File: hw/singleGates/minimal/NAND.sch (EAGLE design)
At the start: 5 parts, among them Q1 BC817, Q2 BC817

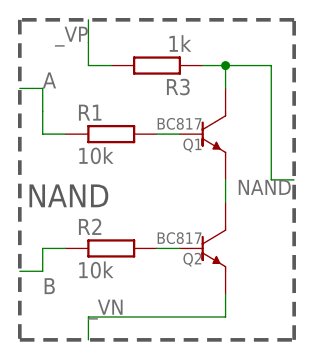
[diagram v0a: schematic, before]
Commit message: Add led output and prepare first alu slice
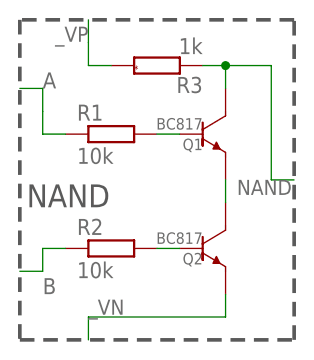
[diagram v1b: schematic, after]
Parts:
- R3: device p.peter-gator:R-EU_R0603 -> p.peter-rcl:R-EU-MARKEDR0603
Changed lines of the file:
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@@
 <part name="R1" library="p.peter-gator" deviceset="R-EU_" device="R0603" value="10k"/>
 <part name="R2" library="p.peter-gator" deviceset="R-EU_" device="R0603" value="10k"/>
-<part name="R3" library="p.peter-gator" deviceset="R-EU_" device="R0603" value="1k"/>
+<part name="R3" library="p.peter-rcl" deviceset="R-EU-MARKED" device="R0603" value="1k"/>
 <part name="Q1" library="p.peter-gator" deviceset="TRANSISTOR-NPN-GENERIC" device="-SOT23-BEC" technology="DEFAULT" value="BC817"/>
 <part name="Q2" library="p.peter-gator" deviceset="TRANSISTOR-NPN-GENERIC" device="-SOT23-BEC" technology="DEFAULT" value="BC817"/>
